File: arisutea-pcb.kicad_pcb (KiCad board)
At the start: 2 copper layers, 339.1 x 121 mm, 186 parts, among them J12 VCC, J13 D+, J14 D-, J15 GND, J16 RGB, J17 RGB_IN, J18 RGB_OUT, J2 MISO, J3 +5V, J4 SCK, J5 MOSI, J6 ~RES~, J7 GND, SW1 SW_Push, SW10 SW_Push, SW11 SW_Push, SW12 SW_Push, SW13 SW_Push, SW14 SW_Push, SW15 SW_Push, SW16 SW_Push, SW17 SW_Push, SW18 SW_Push, SW19 SW_Push, SW2 SW_Push, SW20 SW_Push, SW21 SW_Push, SW22 SW_Push, SW23 SW_Push, SW24 SW_Push, SW25 SW_Push, SW26 SW_Push, SW27 SW_Push, SW28 SW_Push, SW29 SW_Push, SW3 SW_Push, SW30 SW_Push, SW31 SW_Push, SW32 SW_Push, SW33 SW_Push, SW34 SW_Push, SW35 SW_Push, SW36 SW_Push, SW37 SW_Push, SW38 SW_Push, SW39 SW_Push, SW4 SW_Push, SW40 SW_Push, SW41 SW_Push, SW42 SW_Push, SW43 SW_Push, SW44 SW_Push, SW45 SW_Push, SW46 SW_Push, SW47 SW_Push, SW48 SW_Push, SW49 SW_Push, SW5 SW_Push, SW50 SW_Push, SW51 SW_Push, SW52 SW_Push, SW53 SW_Push, SW54 SW_Push, SW55 SW_Push, SW56 SW_Push, SW57 SW_Push, SW58 SW_Push, SW59 SW_Push, SW6 SW_Push, SW60 SW_Push, SW61 SW_Push, SW62 SW_Push, SW63 SW_Push, SW64 SW_Push, SW65 SW_Push, SW66 SW_Push, SW7 SW_Push, SW8 SW_Push, SW9 SW_Push, U1 USBLC6-2SC6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

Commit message: v0.6.3
- Updated mounting holes for new case design.
- Removed matte case as the regular file can be used for either.
- Library update.
- Gerbies regenerated for version bump.
- iBOM added.
- README for most pages edited.
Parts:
- H1, H2, H3, H4, H5, H6, H7, H8: footprint arisutea:Plated_Through_Hole_M2 -> arisutea:Generic-Mounthole
- LOGO3, LOGO4: value arisutea_logo -> QMK Logo; footprint Symbol:OSHW-Logo_11.4x12mm_SilkScreen -> arisutea:OSHW-Logo_11.4x12mm_SilkScreen
- LOGO5, LOGO6: footprint 3x6_graphics:QMK_Logo_Light -> arisutea:QMK_Logo_Light
- renumbered FN to LED1, CAPS to LED2, NUM to LED3
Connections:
- U2 pad 42: Net-(U2-Pad42) -> (no net)
- USB1 pad A8: Net-(USB1-PadA8) -> (no net)
- USB1 pad B8: Net-(USB1-PadB8) -> (no net)
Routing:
- net GND: vias 20 -> 21

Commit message: Version 1.0 Release
Release of version 1.

- Libraries have been merged for easier access.
- Moved one cap a little closer to the MCU.
- Regenerated gerbies, BOM and POS files.
- New iBOM.
- Bumped version number.
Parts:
- J4: value SCK -> SCLK
- U2: value ATmega32U4-AU -> ATMEGA32U4_QFN44
- USB1: value USB_C_HRO_TYPE-C-31-M-12-USB_Type-C -> USB_C_HRO-TYPE-C-31-M-12
- moved J13 2.54 mm to (152.0, 26.3)
- moved J14 2.54 mm to (149.5, 26.3)
- moved C8 1.65 mm to (166.6, 45.7)
- turned C3 to 270 degrees
- turned C4 to 270 degrees
- turned C5 to 0 degrees
- turned R5 to 270 degrees
- turned R6 to 180 degrees
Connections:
- net /MISO renamed MISO
- net /MOSI renamed MOSI
- net /SCK renamed SCLK
- net /col0 renamed col0
- net /col1 renamed col1
- net /col10 renamed col10
- net /col11 renamed col11
- net /col12 renamed col12
- net /col13 renamed col13
- net /col2 renamed col2
- net /col3 renamed col3
- net /col4 renamed col4
- net /col5 renamed col5
- net /col6 renamed col6
- net /col8 renamed col8
- net /col9 renamed col9
- net /row0 renamed row0
- net /row1 renamed row1
- net /row2 renamed row2
- net /row3 renamed row3
- net /row4 renamed row4
- net /~RES~ renamed RESET
- C3 pad 1: +5V -> GND
- C3 pad 2: GND -> +5V
- C4 pad 1: Net-(C4-Pad1) -> GND
- C4 pad 2: GND -> Net-(C4-Pad2)
- C5 pad 1: +5V -> GND
- C5 pad 2: GND -> +5V
- J13 pad 1: Net-(J13-Pad1) -> USB+
- J14 pad 1: Net-(J14-Pad1) -> USB-
- R1 pad 2: Net-(J13-Pad1) -> USB-
- R2 pad 2: Net-(J14-Pad1) -> USB+
- R5 pad 1: Net-(R5-Pad1) -> GND
- R5 pad 2: GND -> Net-(R5-Pad2)
- R6 pad 1: Net-(R6-Pad1) -> GND
- R6 pad 2: GND -> Net-(R6-Pad2)
- U1 pad 4: Net-(J13-Pad1) -> USB-
- U1 pad 6: Net-(J14-Pad1) -> USB+
- U2 pad 6: Net-(C4-Pad1) -> Net-(C4-Pad2)
- USB1 pad A5: Net-(R5-Pad1) -> Net-(R5-Pad2)
- USB1 pad B5: Net-(R6-Pad1) -> Net-(R6-Pad2)
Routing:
- net Net-(R5-Pad2): track 0.00 -> 25.4 mm, vias 0 -> 2
- net Net-(R5-Pad1): track 25.4 -> 0.00 mm, vias 2 -> 0
- net Net-(R6-Pad2): track 0.00 -> 23.1 mm, vias 0 -> 2
- net Net-(R6-Pad1): track 23.1 -> 0.00 mm, vias 2 -> 0
- net USB-: track 0.00 -> 17.7 mm
- net Net-(J13-Pad1): track 17.7 -> 0.00 mm
- net USB+: track 0.00 -> 13.6 mm
- net Net-(J14-Pad1): track 13.6 -> 0.00 mm
- net Net-(C4-Pad2): track 0.00 -> 10.1 mm
- net Net-(C4-Pad1): track 10.1 -> 0.00 mm
- net GND: track 670.4 -> 668.9 mm
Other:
- board text added: "Arisutea Rev 1.0 3x6 Design mattyams"
- board text removed: "Arisutea Rev 0.6 3x6 Design mattyams"

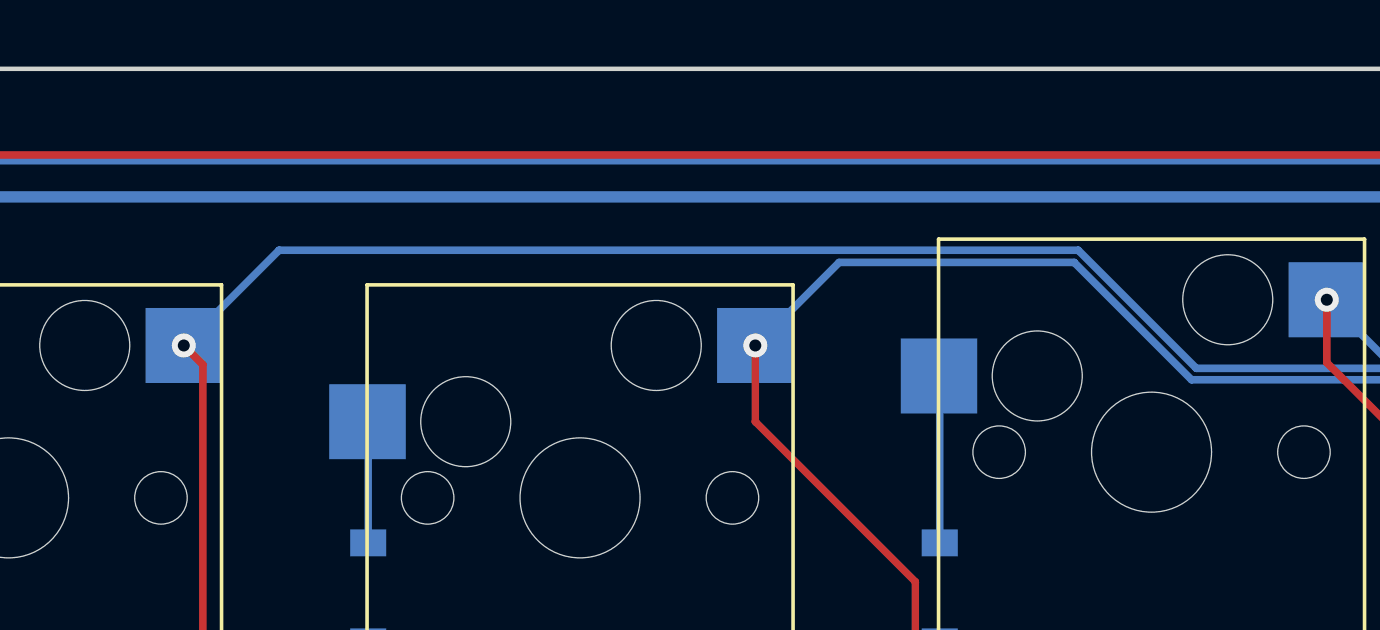
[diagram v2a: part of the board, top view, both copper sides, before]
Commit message: fixed USB net names
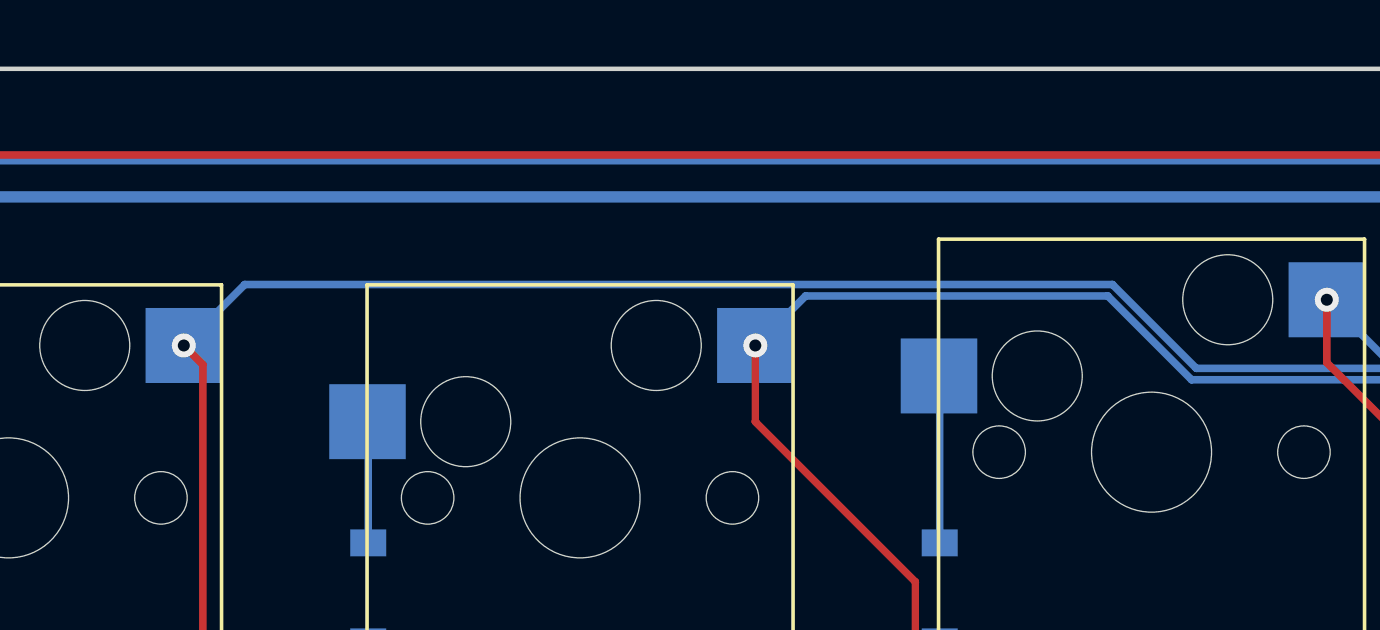
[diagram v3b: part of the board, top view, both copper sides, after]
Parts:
- J13: renamed from J14; value D- -> D+
- J14: renamed from J13; value D+ -> D-
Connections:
- J13 pad 1: USB- -> USB+
- J14 pad 1: USB+ -> USB-
- R1 pad 2: USB- -> USB+
- R2 pad 2: USB+ -> USB-
- U1 pad 4: USB- -> USB+
- U1 pad 6: USB+ -> USB-
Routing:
- net USB-: track 17.7 -> 13.6 mm
- net USB+: track 13.6 -> 17.7 mm
- net col0: track 204.2 -> 203.3 mm
- net col1: track 164.8 -> 163.9 mm
